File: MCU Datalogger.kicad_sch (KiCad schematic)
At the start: 0 parts

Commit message: added required symbol to the schematic sheet
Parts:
- added BT1: Battery, symbol Device:Battery
- added C1, C2, C3, C4: C, symbol Device:C
- added C5: C_Polarized, symbol Device:C_Polarized
- added D1, D2: LED, symbol Device:LED
- added H1, H2, H3, H4: MountingHole, symbol Mechanical:MountingHole
- added R1, R2, R3, R4, R5, R6, R7: R, symbol Device:R
- added U1, U2: 24LC1025, symbol Memory_EEPROM:24LC1025
- added U3: ATMEGA328P-AU, ATMEGA328P-AU:QFP80P900X900X120-32N, symbol ATMEGA328P-AU:ATMEGA328P-AU
- added U4: DS1337S_, DS1337S_:SOIC127P600X175-8N, symbol DS1337S_:DS1337S_
- added Y1, Y2: Crystal, symbol Device:Crystal
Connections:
- new net GND: U3.21 (GND), U3.3 (GND), U3.5 (GND)
- new net VCC: U3.4 (VCC), U3.6 (VCC)
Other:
- added sheet Connectors (connectors.kicad_sch)
- company: (none) -> Nishant Bhardwaj
- title: (none) -> MCU Datalogger with memory and clock

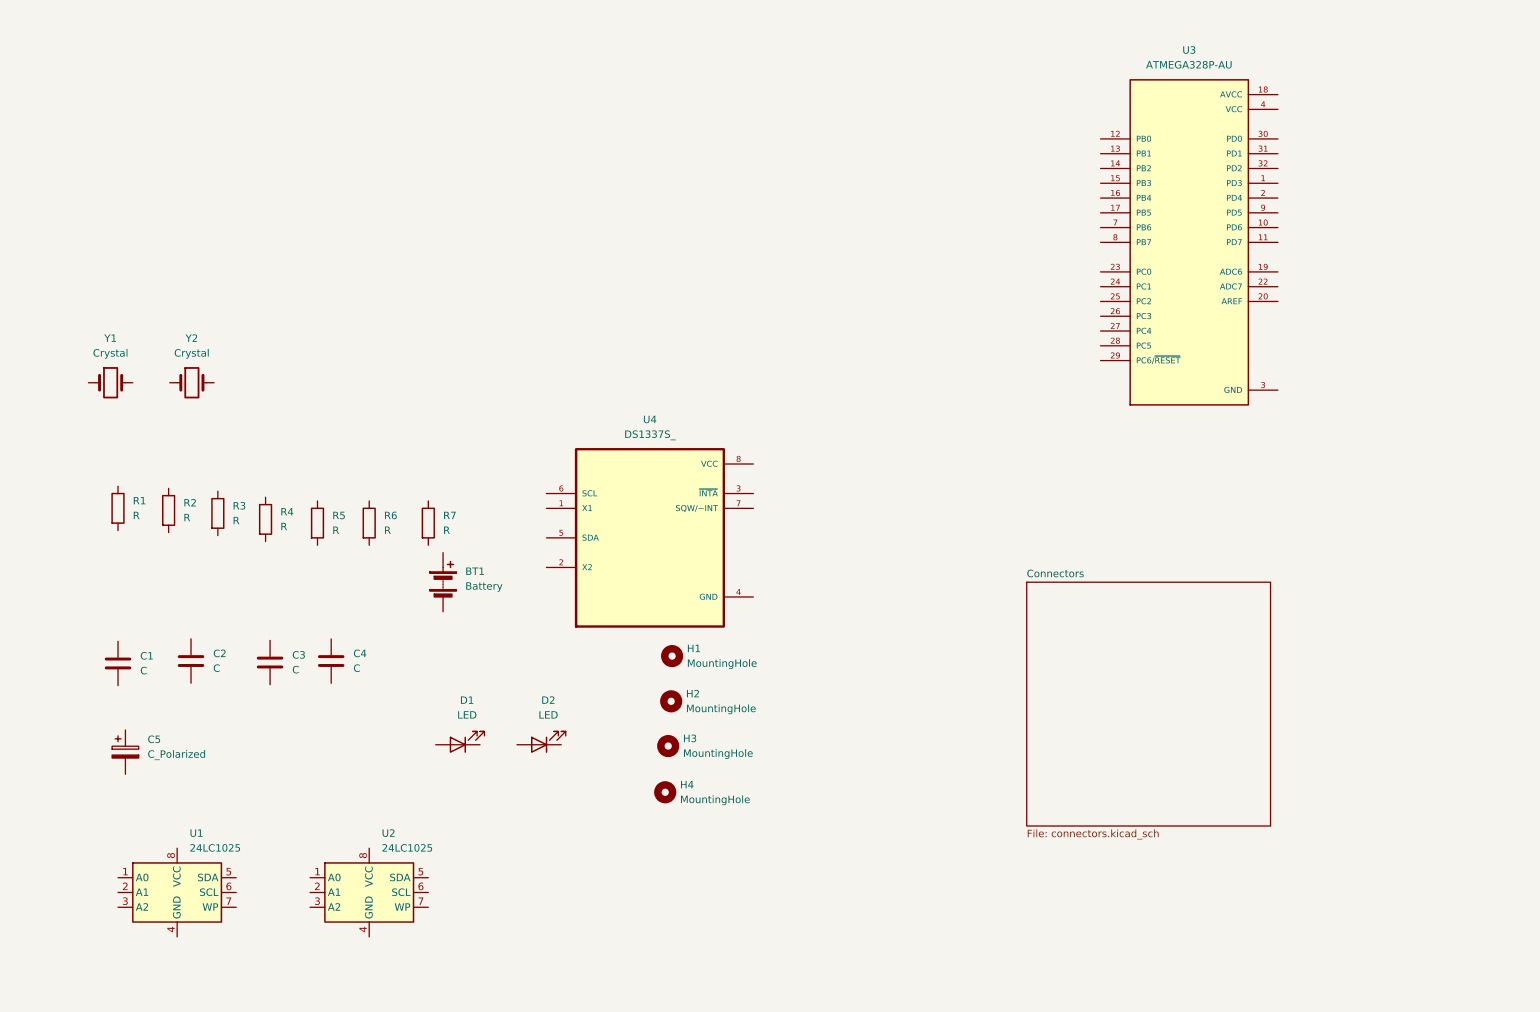
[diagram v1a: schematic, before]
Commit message: changed symbol locations (arranged)
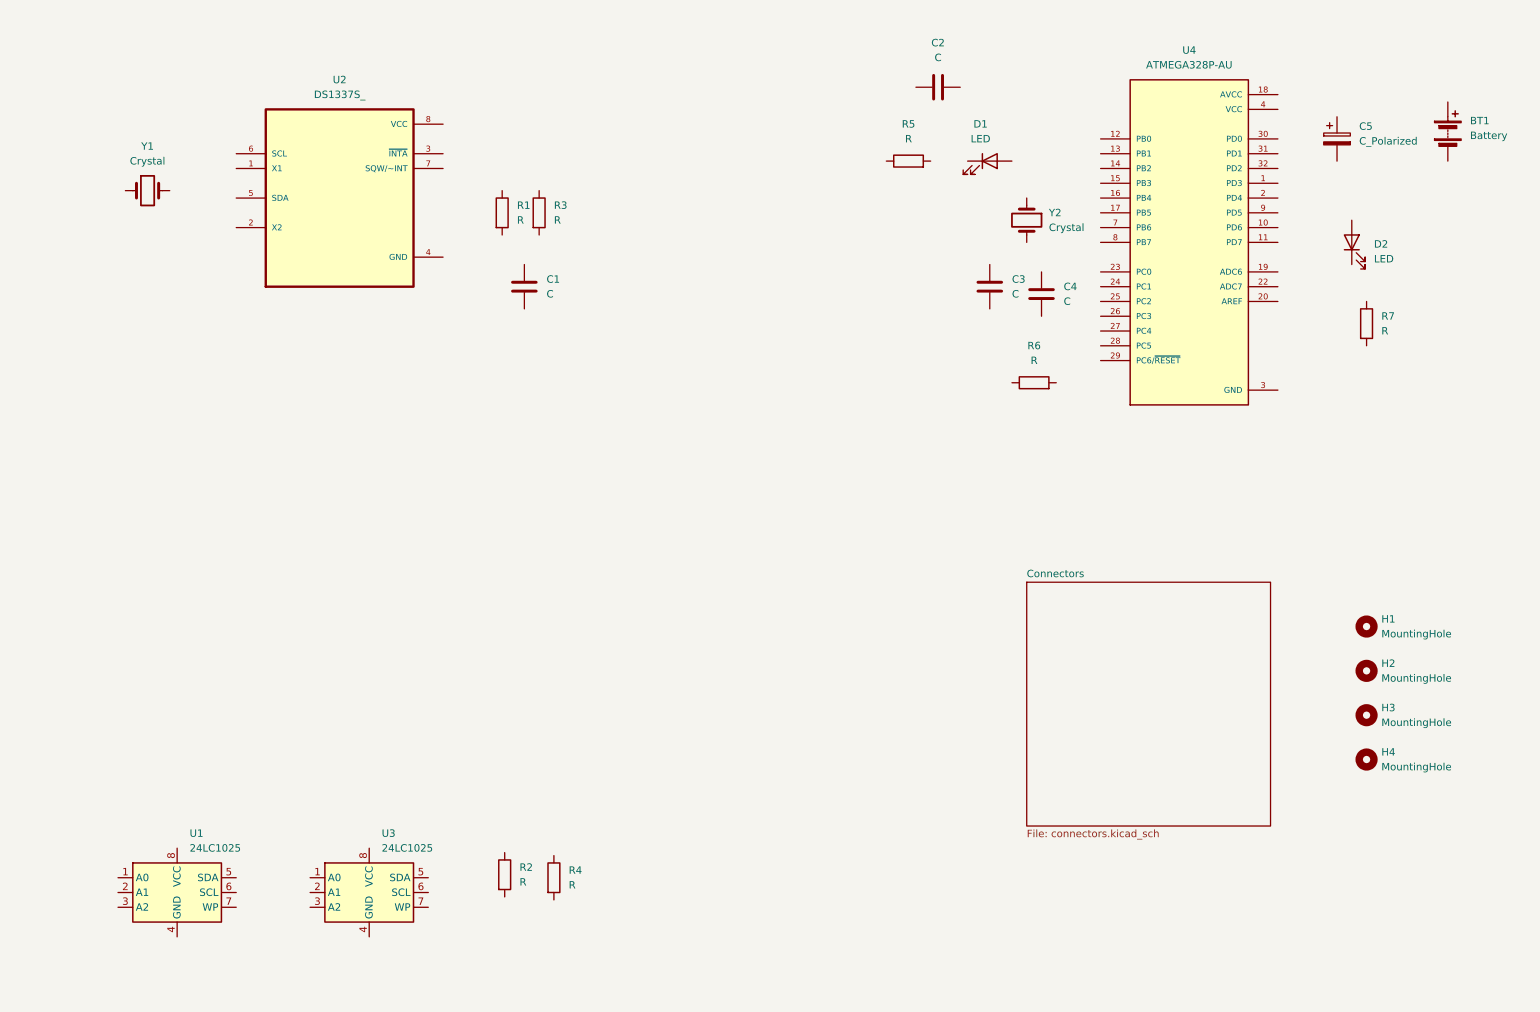
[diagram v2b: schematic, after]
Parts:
- renumbered C4 to C2, C2 to C4, D2 to D1, D1 to D2, R4 to R1, R5 to R3, R3 to R4, R6 to R5, R1 to R6, U4 to U2, U2 to U3, U3 to U4
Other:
- moved on the sheet: BT1, C1, C2, C3, C4, C5, D1, D2, H1, H2, H3, H4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

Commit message: alloted footprints and completed wiring of main sheet
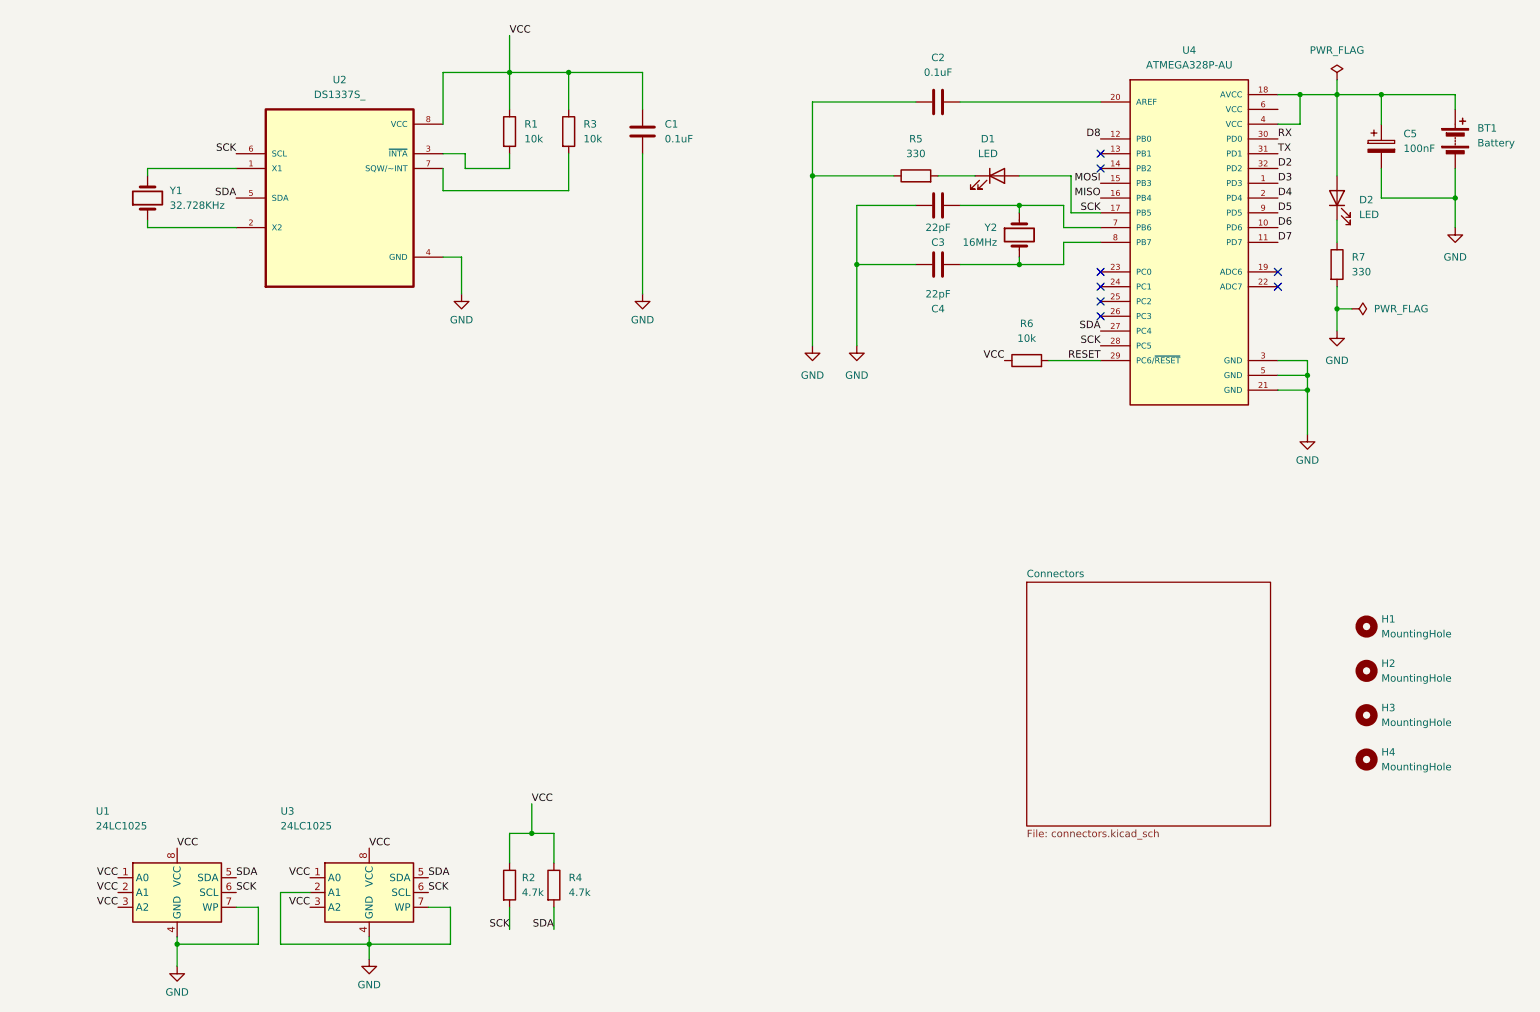
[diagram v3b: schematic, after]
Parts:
- BT1: footprint (none) -> Connector_PinHeader_2.54mm:PinHeader_1x02_P2.54mm_Vertical
- C1, C2: value C -> 0.1uF; footprint (none) -> Capacitor_SMD:C_0805_2012Metric
- C3, C4: value C -> 22pF; footprint (none) -> Capacitor_SMD:C_0805_2012Metric
- C5: value C_Polarized -> 100nF; footprint (none) -> Capacitor_SMD:C_0805_2012Metric
- D1, D2: footprint (none) -> LED_SMD:LED_0805_2012Metric
- H1, H2, H3, H4: footprint (none) -> MountingHole:MountingHole_2.1mm
- R1, R3, R6: value R -> 10k; footprint (none) -> Resistor_SMD:R_0805_2012Metric
- R2, R4: value R -> 4.7k; footprint (none) -> Resistor_SMD:R_0805_2012Metric
- R5, R7: value R -> 330; footprint (none) -> Resistor_SMD:R_0805_2012Metric
- U1, U3: footprint (none) -> soic:SOIC-8_5.23x5.23mm_P1.27mm
- Y1: value Crystal -> 32.728KHz; footprint (none) -> Crystal:Crystal_SMD_5032-2Pin_5.0x3.2mm_HandSoldering
- Y2: value Crystal -> 16MHz; footprint (none) -> Crystal:Crystal_SMD_5032-2Pin_5.0x3.2mm_HandSoldering
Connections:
- net GND: now also BT1.2 (-), C1.2, C2.1, C3.1, C4.2, C5.2, R5.1, R7.2, U1.4 (GND), U1.7 (WP), U2.4 (GND), U3.2 (A1), U3.4 (GND), U3.7 (WP)
- net VCC: now also C1.1, R1.1, R2.1, R3.1, R4.1, R6.1, U1.1 (A0), U1.2 (A1), U1.3 (A2), U1.8 (VCC), U2.8 (VCC), U3.1 (A0), U3.3 (A2), U3.8 (VCC); no longer U4.4 (VCC), U4.6 (VCC)
- net at Y2.1: now also C3.2, U4.7 (PB6)
- net at Y2.2: now also C4.1, U4.8 (PB7)
- net at BT1.1 (+): now also C5.1, D2.2 (A), U4.18 (AVCC), U4.4 (VCC)
- net SDA: now reaches R4.2
- net SDA: now also U1.5 (SDA), U2.5 (SDA), U3.5 (SDA), U4.27 (PC4)
- net SCK: now reaches R2.2
- net SCK: now also D1.2 (A), U1.6 (SCL), U2.6 (SCL), U3.6 (SCL), U4.17 (PB5), U4.28 (PC5)
- net at Y1.1: now also U2.2 (X2)
- net at Y1.2: now also U2.1 (X1)
- net at C2.2: now also U4.20 (AREF)
- net RESET: now reaches R6.2
- net RESET: now also U4.29 (PC6/~{RESET})
- net at U2.3 (~{INTA}): now also R1.2
- net at U2.7 (SQW/~INT): now also R3.2
- net at R7.1: now also D2.1 (K)
- net at D1.1 (K): now also R5.2
- net D3: now reaches U4.1 (PD3)
- net D6: now reaches U4.10 (PD6)
- net D7: now reaches U4.11 (PD7)
- net D8: now reaches U4.12 (PB0)
- net MOSI: now reaches U4.15 (PB3)
- net MISO: now reaches U4.16 (PB4)
- net D4: now reaches U4.2 (PD4)
- net RX: now reaches U4.30 (PD0)
- net TX: now reaches U4.31 (PD1)
- net D2: now reaches U4.32 (PD2)
- net D5: now reaches U4.9 (PD5)
- no-connect marks 0 -> 8
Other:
- moved on the sheet: BT1, C1, C2, C3, C4, C5, D1, D2, R1, R2, R3, R4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

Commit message: completed the wiring of sheet 2 and allocated power net class to GND and VCC
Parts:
- U2: footprint DS1337S_:SOIC127P600X175-8N -> ATMEGA328P-AU:SOIC127P600X175-8N
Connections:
- no-connect marks 8 -> 9
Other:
- sheet Connectors ports: added D2, D3, D4, D5, D6, D7, D8, GND, MISO, MOSI, RESET, RX, SCK, SDA, TX, VCC; removed none
- moved on the sheet: R2, R4, U1, U3

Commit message: added comments
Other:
- note added: "EEPROM"
- note added: "MCU"
- note added: "Mounting"
- note added: "Real time clock"
- moved on the sheet: BT1, C1, C2, C3, C4, C5, D1, D2, H1, H2, H3, H4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
